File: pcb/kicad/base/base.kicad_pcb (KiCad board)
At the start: 2 copper layers, 41 parts, among them P1 J-Link SWD, P2 SMA, P3 Power Source, U1 SAMB11G18A-edit, U2 XBee-PRO_900HP, Y1 32.768kHz, Y2 26MHz

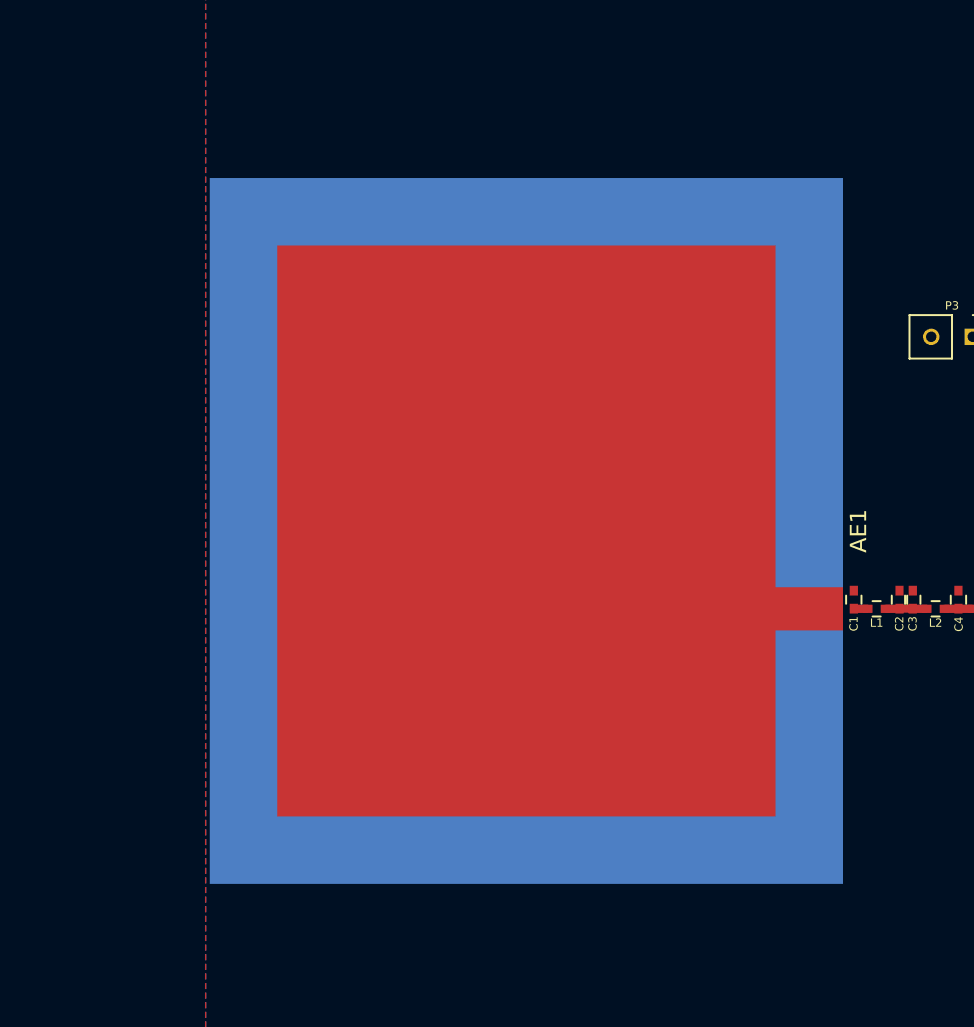
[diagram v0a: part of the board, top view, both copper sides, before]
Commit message: Add new tests for patch antenna
Two new test boards laid out to test impedance and performance due to
the effect of larger copper void space in the presence of nearby ground
copper, one board with a matching circuit and the other without. Traces
no longer follow the optimal transmission line width for 50ohm
performance due to the use of 0402 SMD technology.
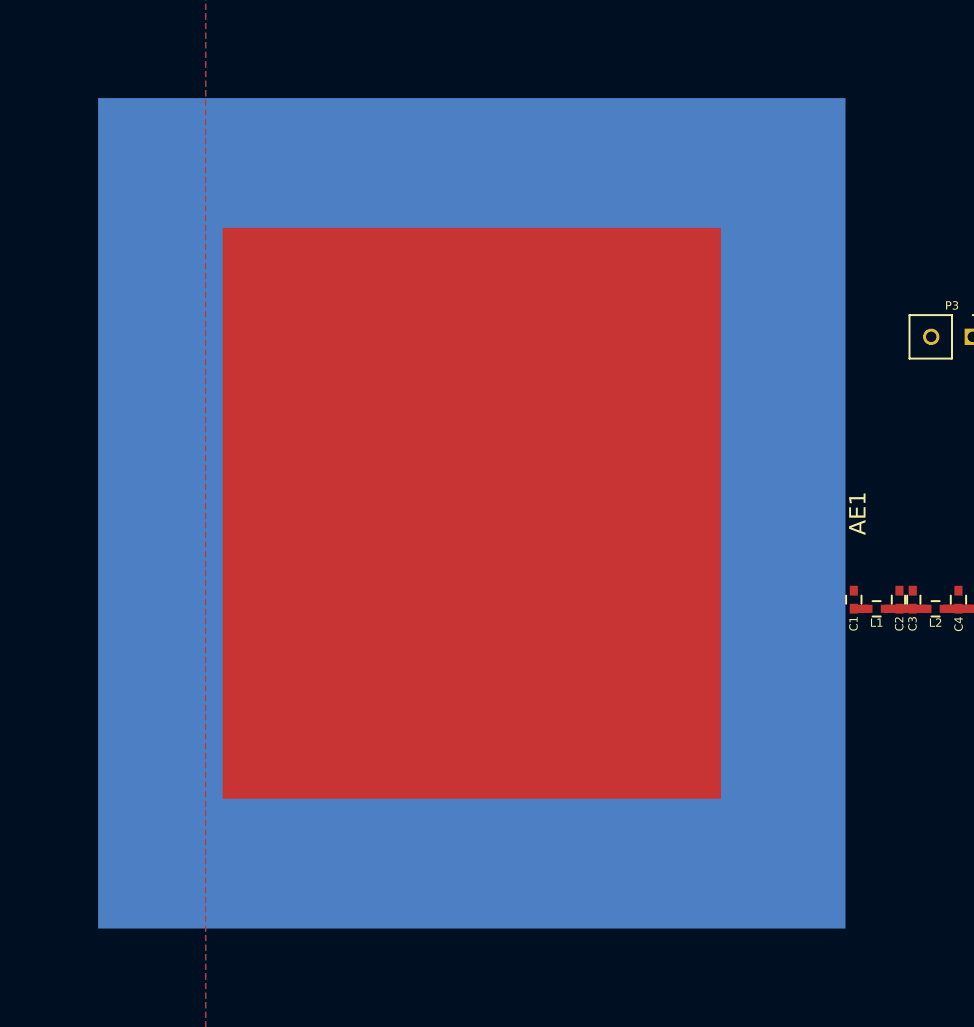
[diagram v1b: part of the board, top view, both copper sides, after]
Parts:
- AE1: value 2.4-2.4835GHz -> Antenna_Shield
- moved AE1 3.51 mm to (111.3, 81.7)
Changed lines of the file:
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@@
-(kicad_pcb (version 4) (host pcbnew 4.0.6)
+(kicad_pcb (version 4) (host pcbnew 4.0.5)
   (general
-    (links 153)
-    (no_connects 33)
+    (links 152)
+    (no_connects 32)
     (area 0 0 0 0)
     (thickness 1.6)
@@
   )
   (setup
-    (last_trace_width 0.762)
+    (last_trace_width 0.254)
     (user_trace_width 0.254)
     (user_trace_width 0.508)
@@
   )
   (module Antennas:Patch_Antenna_2.4GHz (layer F.Cu)
-    (at 114.6175 82.7405 90)
+    (at 111.2774 81.661 90)
     (descr "2.4GHz Patch Antenna")
     (tags "antenna patch 2.4")
-    (fp_text reference AE1 (at 0 20.32 90) (layer F.SilkS)
-      (effects (font (size 1 1) (thickness 0.15)))
-    )
-    (fp_text value 2.4-2.4835GHz (at 0 -20.32 90) (layer F.Fab)
-      (effects (font (size 1 1) (thickness 0.15)))
-    )
-    (pad 2 smd rect (at 0 0 90) (size 43.18 38.735) (layers B.Cu)
-      (net 2 GND))
+    (fp_text reference AE1 (at 0 23.622 90) (layer F.SilkS)
+      (effects (font (size 1 1) (thickness 0.15)))
+    )
+    (fp_text value Antenna_Shield (at 0 -23.622 90) (layer F.Fab)
+      (effects (font (size 1 1) (thickness 0.15)))
+    )
+    (pad 2 smd rect (at 0 0 90) (size 50.8 45.72) (layers B.Cu)
+      (net 2 GND) (zone_connect 0))
     (pad 1 smd rect (at 0 0 90) (size 34.925 30.48) (layers F.Cu)
-      (net 1 /SIG_2.4G))
-    (pad 1 smd rect (at -4.7625 17.30375 90) (size 2.6416 4.1275) (layers F.Cu)
-      (net 1 /SIG_2.4G))
+      (net 1 /SIG_2.4G) (zone_connect 0))
   )
   (gr_text 0.2 (at 270.51 193.04) (layer Cmts.User)

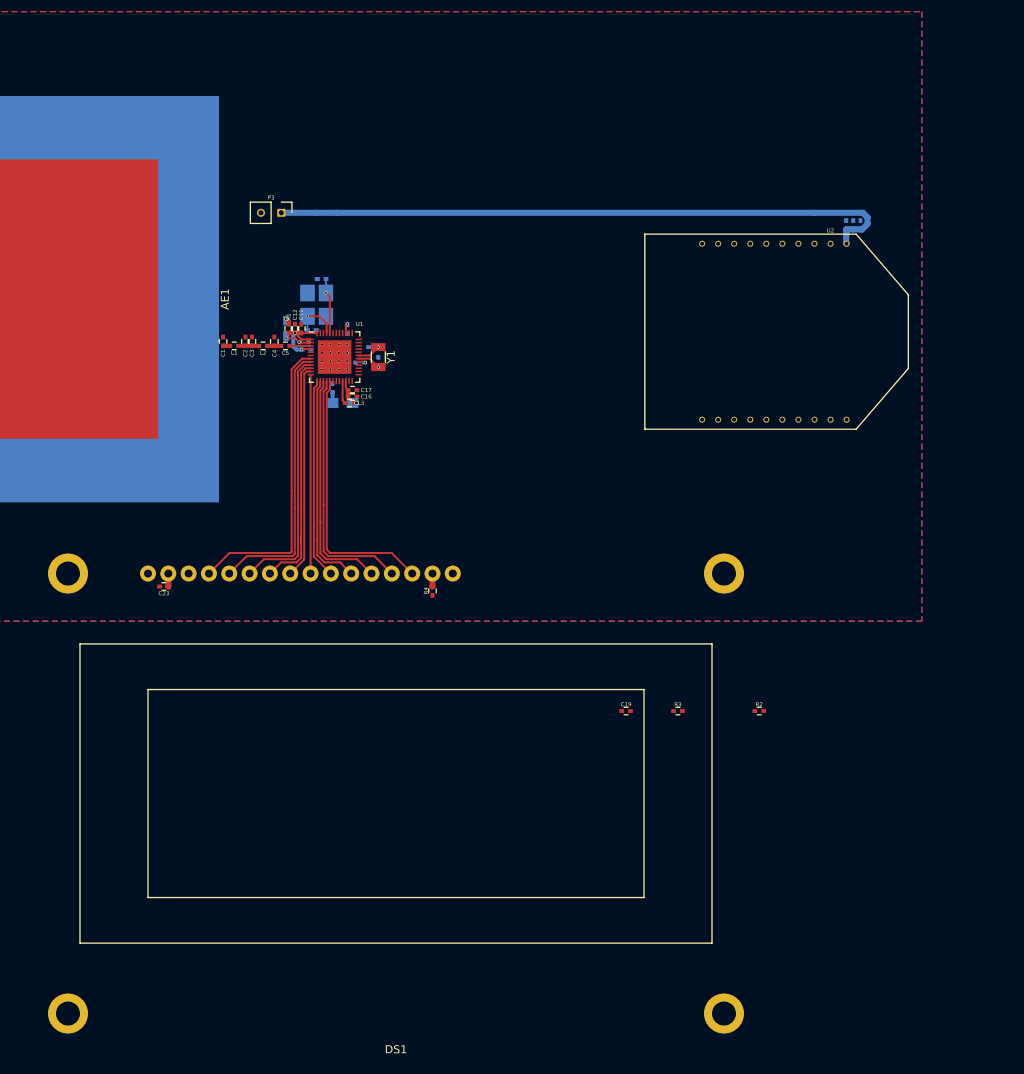
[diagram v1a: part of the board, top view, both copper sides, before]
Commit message: Update display and XBee position
Display is now placed on top of uC to shrink total package dimensions
and the XBee has been moved to accompany this change. Net vias have
been fixed to fit Bay Area Circuits' design constraints.
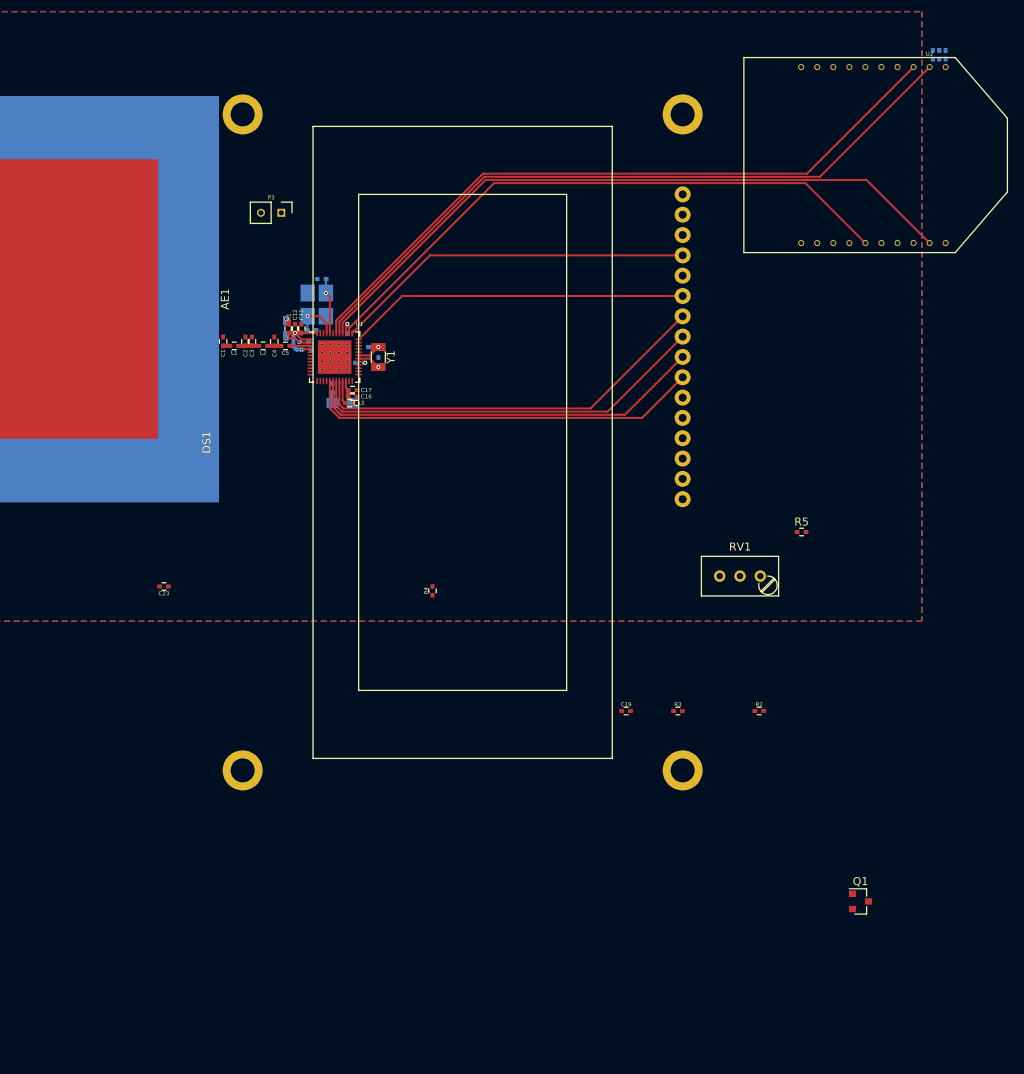
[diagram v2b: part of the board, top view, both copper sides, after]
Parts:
- added Q1: IRLML2502, TO_SOT_Packages_SMD:SOT-23, F.Cu at (214.3, 156.9)
- added R5: 1k, Capacitors_SMD:C_0402, F.Cu at (207.0, 110.8)
- added RV1: 10k, Potentiometers:Potentiometer_Trimmer_Bourns_3296W, F.Cu at (201.8, 116.3)
- moved DS1 44.7 mm to (164.6, 99.6), turned to 270 degrees
- moved U2 25.3 mm to (222.6, 63.7)
- moved C20 23.9 mm to (223.4, 51.1)
- moved C21 23.8 mm to (224.2, 51.1)
- moved C22 23.8 mm to (225.0, 51.1)
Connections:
- DS1 pad 11: /DISP_B4 -> /base-display/DATA_4
- DS1 pad 12: /DISP_B5 -> /base-display/DATA_5
- DS1 pad 13: /DISP_B6 -> /base-display/DATA_6
- DS1 pad 14: /DISP_B7 -> /base-display/DATA_7
- DS1 pad 16: GND -> Net-(DS1-Pad16)
- DS1 pad 3: /base-display/DISP_LGHT -> Net-(DS1-Pad3)
- DS1 pad 5: /DISP_RW -> GND
- P1 pad 19: /+5V -> /+5V_DEBUG
- U1 pad 10: /DISP_B0 -> Net-(U1-Pad10)
- U1 pad 11: /DISP_B1 -> Net-(U1-Pad11)
- U1 pad 12: /DISP_B2 -> Net-(U1-Pad12)
- U1 pad 13: /DISP_B3 -> Net-(U1-Pad13)
- U1 pad 14: /DISP_B4 -> Net-(U1-Pad14)
- U1 pad 15: /DISP_B5 -> Net-(U1-Pad15)
- U1 pad 16: /DISP_B6 -> /DISP_CTRST
- U1 pad 17: /DISP_B7 -> /DISP_B3
- U1 pad 18: Net-(U1-Pad18) -> /DISP_B2
- U1 pad 19: Net-(U1-Pad19) -> /DISP_B1
- U1 pad 20: Net-(U1-Pad20) -> /DISP_B0
- U1 pad 36: /UART_RTS -> /DISP_E
- U1 pad 37: /UART_CTS -> /DISP_REG
- U1 pad 38: /UART_RX -> /UART_RTS
- U1 pad 40: /UART_TX -> /UART_CTS
- U1 pad 41: GND -> /UART_RX
- U1 pad 42: GND -> /UART_TX
- U1 pad 7: /DISP_REG -> Net-(U1-Pad7)
- U1 pad 8: /DISP_RW -> Net-(U1-Pad8)
- U1 pad 9: /DISP_E -> Net-(U1-Pad9)
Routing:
- net /UART_RX: track 0.00 -> 88.4 mm
- net /UART_TX: track 0.00 -> 86.9 mm
- net /UART_CTS: track 0.00 -> 85.3 mm
- net /+3.3V: track 82.4 -> 3.28 mm
- net /UART_RTS: track 0.00 -> 75.8 mm
- net /DISP_RW: track 34.6 -> 0.00 mm
- net /DISP_B7: track 33.1 -> 0.00 mm
- net /DISP_B6: track 31.1 -> 0.00 mm
- net /DISP_B5: track 29.1 -> 0.00 mm
- net /DISP_B4: track 27.1 -> 0.00 mm
- net /DISP_B2: track 24.9 -> 50.3 mm
- net /DISP_B3: track 25.1 -> 50.1 mm
- net /DISP_B1: track 26.6 -> 50.6 mm
- net /DISP_B0: track 29.3 -> 50.8 mm
- net /DISP_E: track 31.9 -> 42.8 mm
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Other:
- net class Default: via_dia 0.381 -> 0.508
- net class Power: via_dia 0.508 -> 0.762; via_drill 0.381 -> 0.508

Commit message: Fix power and display routing with proper via size
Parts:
- R2: moved to B.Cu
- moved R2 86.8 mm to (116.6, 115.9), turned to 90 degrees
- moved R3 80.5 mm to (117.0, 102.7), turned to 270 degrees
- moved Q1 74.4 mm to (173.2, 95.0), turned to 90 degrees
- moved C23 57.5 mm to (179.7, 94.0), turned to 90 degrees
- moved R5 39.4 mm to (170.4, 96.0)
- moved P3 38.8 mm to (128.4, 34.5)
- moved P1 36.4 mm to (115.7, 98.7)
- moved R4 30.2 mm to (178.3, 93.5), turned to 180 degrees
- moved RV1 29.6 mm to (182.9, 93.5), turned to 270 degrees
- moved C10 26.0 mm to (126.3, 69.9)
- moved C14 26.0 mm to (129.8, 74.6)
- moved C20 26.0 mm to (204.8, 33.0)
- moved C22 26.0 mm to (206.4, 33.0)
- moved C7 26.0 mm to (134.8, 69.5)
- moved C8 26.0 mm to (128.4, 61.0)
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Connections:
- DS1 pad 10: /DISP_B3 -> /base-display/DATA_3
- DS1 pad 11: /base-display/DATA_4 -> /DISP_B0
- DS1 pad 12: /base-display/DATA_5 -> /DISP_B1
- DS1 pad 13: /base-display/DATA_6 -> /DISP_B2
- DS1 pad 14: /base-display/DATA_7 -> /DISP_B3
- DS1 pad 7: /DISP_B0 -> /base-display/DATA_0
- DS1 pad 8: /DISP_B1 -> /base-display/DATA_1
- DS1 pad 9: /DISP_B2 -> /base-display/DATA_2
- U1 pad 14: Net-(U1-Pad14) -> /DISP_CTRST
- U1 pad 15: Net-(U1-Pad15) -> /DISP_B3
- U1 pad 16: /DISP_CTRST -> /DISP_B2
- U1 pad 17: /DISP_B3 -> /DISP_B1
- U1 pad 18: /DISP_B2 -> /DISP_B0
- U1 pad 19: /DISP_B1 -> /DISP_E
- U1 pad 20: /DISP_B0 -> /DISP_REG
- U1 pad 36: /DISP_E -> GND
- U1 pad 37: /DISP_REG -> GND
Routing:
- net Net-(P1-Pad15): track 0.00 -> 55.7 mm, vias 0 -> 3
- net /SWDCLK: track 0.00 -> 45.4 mm
- net /SWDIO: track 0.00 -> 44.3 mm, vias 0 -> 1
- net /+3.3V: track 3.28 -> 21.5 mm, vias 1 -> 2
- net /DISP_E: track 42.8 -> 52.1 mm
- net /DISP_REG: track 45.3 -> 53.4 mm
- net /DISP_B3: track 50.1 -> 56.8 mm
- net /DISP_B2: track 50.3 -> 55.3 mm
- net /UART_RX: track 88.4 -> 84.1 mm
- net /UART_TX: track 86.9 -> 82.6 mm
- net /UART_RTS: track 75.8 -> 71.5 mm
- net /UART_CTS: track 85.3 -> 81.1 mm
- net /+5V: track 0.00 -> 4.09 mm
- net Net-(C10-Pad1): track 10.0 -> 6.44 mm, vias 2 -> 1
- net /DISP_B1: track 50.6 -> 53.7 mm
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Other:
- net class Default: clearance 0.127 -> 0.1397
- net class Power: clearance 0.127 -> 0.1397
- rule trace_clearance: 0.127 -> 0.1397

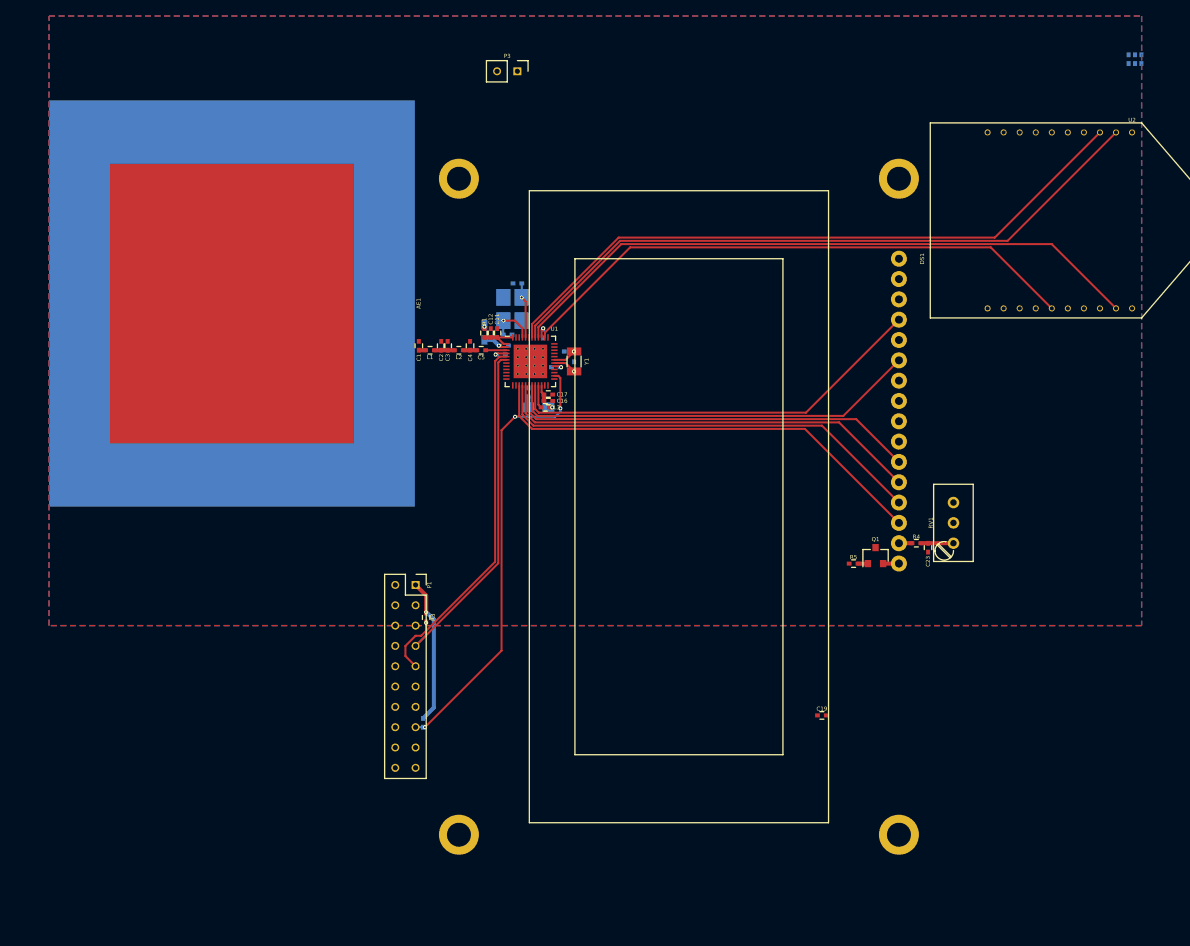
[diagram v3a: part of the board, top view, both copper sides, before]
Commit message: Add USB micro B receptacle footprint
USB B footprint generated for potential data/debugging connection.
XBee could potentially move to bottom right corner of layout by using
UART pins near the bottom of the uC (12-20) and moving the display pins
to the top (36-42). Speaker can be placed directly to the above (to the
right in layout) the display.
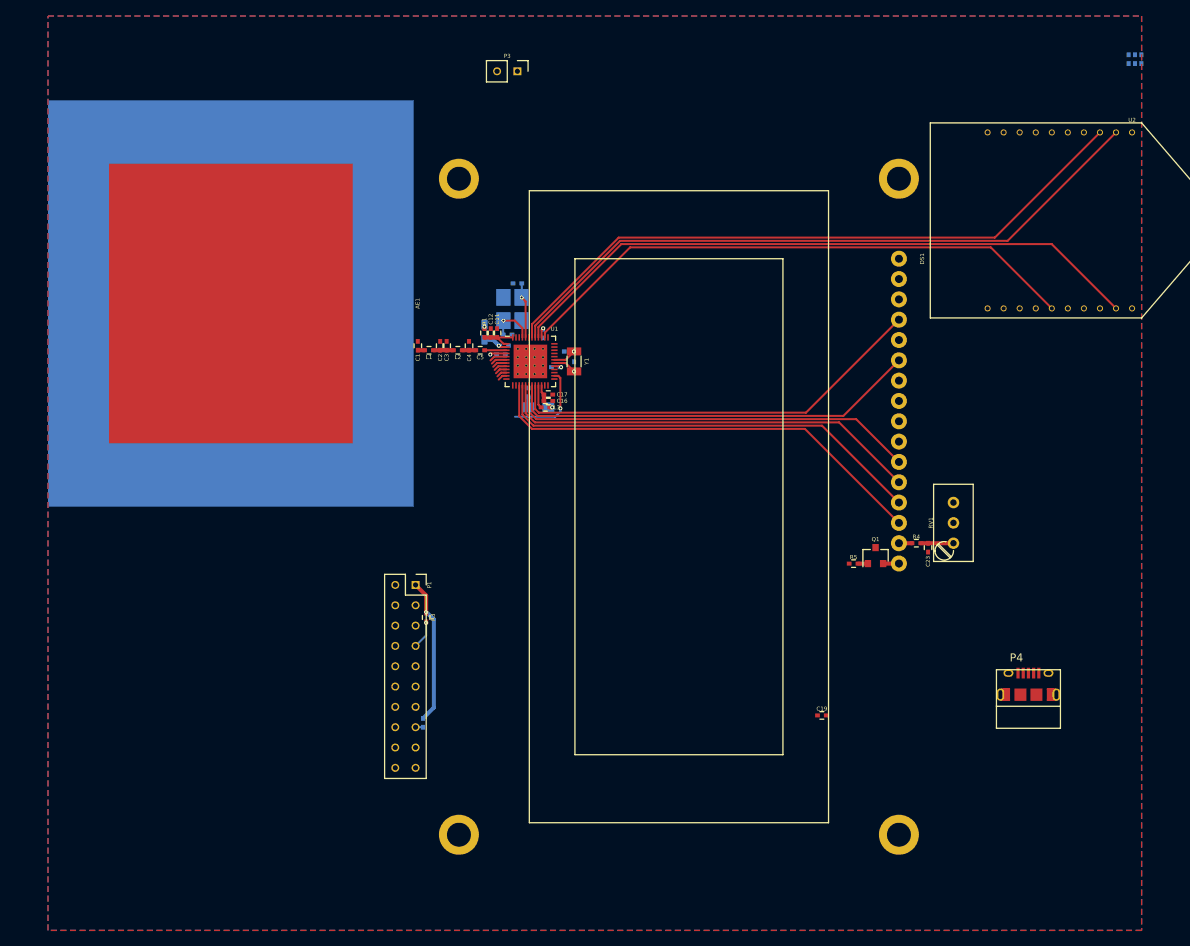
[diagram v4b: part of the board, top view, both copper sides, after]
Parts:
- added P4: USB Micro B, Connectors:USB_Micro-B_10118194-000XLF, F.Cu at (192.3, 112.4)
- moved C1 0.13 mm to (116.0, 68.8)
- moved C4 0.13 mm to (122.4, 68.8)
- moved AE1 0.13 mm to (92.6, 63.5)
- moved C2 0.13 mm to (118.7, 68.8)
- moved C3 0.13 mm to (119.6, 68.8)
- moved C5 0.13 mm to (123.7, 69.3)
- moved L1 0.13 mm to (117.3, 69.3)
- moved L2 0.13 mm to (121.0, 69.3)
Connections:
- U1 pad 7: Net-(U1-Pad7) -> /Data-
- U1 pad 8: Net-(U1-Pad8) -> /Data+
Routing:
- net Net-(P1-Pad15): track 55.7 -> 11.9 mm, vias 3 -> 1
- net /SWDCLK: track 45.4 -> 2.19 mm
- net /SWDIO: track 44.3 -> 5.45 mm
- net /Data-: track 0.00 -> 1.84 mm
- net /Data+: track 0.00 -> 1.66 mm
- net Net-(U1-Pad9): track 0.00 -> 1.50 mm
- net Net-(U1-Pad10): track 0.00 -> 1.32 mm
- net Net-(U1-Pad11): track 0.00 -> 1.16 mm
- net Net-(C10-Pad1): track 6.44 -> 7.12 mm
